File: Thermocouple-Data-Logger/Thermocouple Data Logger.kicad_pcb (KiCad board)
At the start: 4 copper layers, 0 parts

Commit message: Imported all the parts
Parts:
- added C0: 14pF, Capacitors_SMD:C_0402, F.Cu at (201.3, 115.1)
- added C1: 14pF, Capacitors_SMD:C_0402, F.Cu at (205.5, 115.1)
- added C10: 0.01uF, Capacitors_SMD:C_0402, F.Cu at (252.1, 46.7)
- added C11: 0.01uF, Capacitors_SMD:C_0402, F.Cu at (223.6, 72.4)
- added C12: 0.01uF, Capacitors_SMD:C_0402, F.Cu at (220.0, 103.8)
- added C13: 0.1uF, Capacitors_SMD:C_0603, F.Cu at (182.8, 100.7)
- added C14: 0.1uF, Capacitors_SMD:C_0603, F.Cu at (139.4, 124.8)
- added C15: 0.1uF, Capacitors_SMD:C_0603, F.Cu at (257.3, 56.1)
- added C16: 0.1uF, Capacitors_SMD:C_0603, F.Cu at (262.9, 52.0)
- added C17: 0.1uF, Capacitors_SMD:C_0603, F.Cu at (250.8, 61.6)
- added C18: 0.1uF, Capacitors_SMD:C_0603, F.Cu at (240.0, 72.6)
- added C19: 0.1uF, Capacitors_SMD:C_0603, F.Cu at (160.7, 86.8)
- added C2: 18pF, Capacitors_SMD:C_0402, F.Cu at (169.1, 116.4)
- added C20: 0.1uF, Capacitors_SMD:C_0603, F.Cu at (173.5, 86.7)
- added C21: 0.33uF, Capacitors_SMD:C_0603, F.Cu at (169.0, 106.5)
- added C22: 0.33uF, Capacitors_SMD:C_0603, F.Cu at (174.7, 106.5)
- added C23: 0.33uF, Capacitors_SMD:C_0603, F.Cu at (168.9, 111.6)
- added C24: 0.33uF, Capacitors_SMD:C_0603, F.Cu at (162.8, 114.8)
- added C25: 0.33uF, Capacitors_SMD:C_0603, F.Cu at (246.5, 47.0)
- added C26: 0.33uF, Capacitors_SMD:C_0603, F.Cu at (245.7, 63.5)
- added C27: 0.33uF, Capacitors_SMD:C_0603, F.Cu at (252.1, 56.6)
- added C28: 0.33uF, Capacitors_SMD:C_0603, F.Cu at (212.3, 72.6)
- added C29: 0.33uF, Capacitors_SMD:C_0603, F.Cu at (263.4, 47.0)
- added C3: 18pF, Capacitors_SMD:C_0402, F.Cu at (179.6, 110.4)
- added C30: 0.33uF, Capacitors_SMD:C_0603, F.Cu at (252.1, 51.5)
- added C31: 0.33uF, Capacitors_SMD:C_0603, F.Cu at (245.7, 68.5)
- added C32: 0.33uF, Capacitors_SMD:C_0603, F.Cu at (217.9, 72.6)
- added C33: 0.33uF, Capacitors_SMD:C_0603, F.Cu at (177.7, 100.7)
- added C34: 0.33uF, Capacitors_SMD:C_0603, F.Cu at (155.9, 123.3)
- added C35: 0.33uF, Capacitors_SMD:C_0603, F.Cu at (172.7, 70.1)
- added C36: 0.33uF, Capacitors_SMD:C_0603, F.Cu at (181.1, 65.3)
- added C37: 0.33uF, Capacitors_SMD:C_0603, F.Cu at (172.7, 75.1)
- added C38: 0.33uF, Capacitors_SMD:C_0603, F.Cu at (161.2, 81.7)
- added C39: 0.33uF, Capacitors_SMD:C_0603, F.Cu at (199.4, 47.0)
- added C4: 0.01uF, Capacitors_SMD:C_0402, F.Cu at (257.8, 51.3)
- added C40: 10uF, Capacitors_SMD:C_1210, F.Cu at (204.2, 105.9)
- added C41: 22uf, Capacitors_SMD:C_1206, F.Cu at (214.7, 104.2)
- added C5: 0.01uF, Capacitors_SMD:C_0402, F.Cu at (234.8, 72.4)
- added C6: 0.01uF, Capacitors_SMD:C_0402, F.Cu at (257.8, 46.7)
- added C7: 0.01uF, Capacitors_SMD:C_0402, F.Cu at (246.5, 56.4)
- added C8: 0.01uF, Capacitors_SMD:C_0402, F.Cu at (229.2, 72.4)
- added C9: 0.01uF, Capacitors_SMD:C_0402, F.Cu at (246.5, 51.8)
- added D0: LED Power, LEDs:LED_0603, F.Cu at (161.8, 109.9)
- added D1: LED Debug, LEDs:LED_0603, F.Cu at (161.9, 105.2)
- added D10: D_Schottky, Diodes_SMD:D_SOD-323, F.Cu at (179.1, 95.3)
- added D11: D_Schottky, Diodes_SMD:D_SOD-323, F.Cu at (170.4, 101.1)
- added D2: LED Probe 1, LEDs:LED_0603, F.Cu at (174.9, 46.7)
- added D3: LED Probe 2, LEDs:LED_0603, F.Cu at (174.9, 51.4)
- added D4: LED Probe 3, LEDs:LED_0603, F.Cu at (174.9, 56.0)
- added D5: LED Probe 4, LEDs:LED_0603, F.Cu at (155.0, 76.8)
- added D6: LED °C, LEDs:LED_0603, F.Cu at (162.9, 76.8)
- added D7: LED °F, LEDs:LED_0603, F.Cu at (191.1, 55.9)
- added D8: LED K, LEDs:LED_0603, F.Cu at (199.3, 79.4)
- added D9: D_Schottky, Diodes_SMD:D_SOD-323, F.Cu at (170.4, 95.3)
- added J0: Power, Connectors_JST:JST_PH_S2B-PH-SM4-TB_02x2.00mm_Angled, F.Cu at (196.9, 99.1)
- added J1: Micro_SD_Card_Det, Connectors_Card:Hirose_DM3BT-DSF-PEJS, F.Cu at (87.0, 84.0)
- added J2: Probe 1, TerminalBlock-PTSA:TeaminalBlock_Phonix_PTSA-3.5mm_2pol, F.Cu at (85.0, 30.0)
- added J3: Probe 2, TerminalBlock-PTSA:TeaminalBlock_Phonix_PTSA-3.5mm_2pol, F.Cu at (105.0, 30.0)
- added J4: Probe 3, TerminalBlock-PTSA:TeaminalBlock_Phonix_PTSA-3.5mm_2pol, F.Cu at (125.0, 30.0)
- added J5: Probe 4, TerminalBlock-PTSA:TeaminalBlock_Phonix_PTSA-3.5mm_2pol, F.Cu at (145.0, 30.0)
- added J6: ISP, Pin_Headers:Pin_Header_Straight_2x03_Pitch2.54mm, F.Cu at (85.0, 107.3)
- added R0: 100, Resistors_SMD:R_0603, F.Cu at (254.9, 61.6)
- added R1: 100, Resistors_SMD:R_0603, F.Cu at (244.1, 73.5)
- added R10: 200, Resistors_SMD:R_0805, F.Cu at (161.7, 120.0)
- added R11: 200, Resistors_SMD:R_0805, F.Cu at (192.7, 66.4)
- added R12: 200, Resistors_SMD:R_0805, F.Cu at (187.9, 71.8)
- added R13: 200, Resistors_SMD:R_0805, F.Cu at (202.8, 58.0)
- added R14: 200, Resistors_SMD:R_0805, F.Cu at (177.3, 70.5)
- added R15: 200, Resistors_SMD:R_0805, F.Cu at (181.8, 81.8)
- added R16: 200, Resistors_SMD:R_0805, F.Cu at (196.3, 68.5)
- added R17: 200, Resistors_SMD:R_0805, F.Cu at (191.5, 71.8)
- added R18: 200, Resistors_SMD:R_0805, F.Cu at (187.9, 77.3)
- added R19: 200, Resistors_SMD:R_0805, F.Cu at (199.8, 63.5)
- added R2: 100, Resistors_SMD:R_0603, F.Cu at (250.2, 71.6)
- added R20: 200, Resistors_SMD:R_0805, F.Cu at (203.4, 63.5)
- added R21: 200, Resistors_SMD:R_0805, F.Cu at (199.8, 68.9)
- added R22: 200, Resistors_SMD:R_0805, F.Cu at (191.5, 77.3)
- added R23: 200, Resistors_SMD:R_0805, F.Cu at (195.0, 74.0)
- added R24: 200, Resistors_SMD:R_0805, F.Cu at (185.3, 82.7)
- added R25: 200, Resistors_SMD:R_0805, F.Cu at (203.4, 68.9)
- added R26: 200, Resistors_SMD:R_0805, F.Cu at (188.9, 82.7)
- added R27: 200, Resistors_SMD:R_0805, F.Cu at (198.6, 74.4)
- added R28: 200, Resistors_SMD:R_0805, F.Cu at (195.0, 79.4)
- added R29: 200, Resistors_SMD:R_0805, F.Cu at (202.1, 74.4)
- added R3: 100, Resistors_SMD:R_0603, F.Cu at (250.2, 66.6)
- added R30: 200, Resistors_SMD:R_0805, F.Cu at (169.3, 85.8)
- added R31: 200, Resistors_SMD:R_0805, F.Cu at (204.0, 47.1)
- added R32: 200, Resistors_SMD:R_0805, F.Cu at (198.4, 52.2)
- added R33: 200, Resistors_SMD:R_0805, F.Cu at (190.0, 60.9)
- added R34: 200, Resistors_SMD:R_0805, F.Cu at (185.6, 65.4)
- added R35: 200, Resistors_SMD:R_0805, F.Cu at (165.8, 82.7)
- added R36: 200, Resistors_SMD:R_0805, F.Cu at (196.3, 63.1)
- added R37: 200, Resistors_SMD:R_0805, F.Cu at (178.2, 81.4)
- added R38: 200, Resistors_SMD:R_0805, F.Cu at (184.4, 76.3)
- added R39: 200, Resistors_SMD:R_0805, F.Cu at (174.7, 81.4)
- added R4: 100, Resistors_SMD:R_0603, F.Cu at (261.3, 57.0)
- added R40: 200, Resistors_SMD:R_0805, F.Cu at (202.8, 52.6)
- added R41: 200, Resistors_SMD:R_0805, F.Cu at (180.8, 75.9)
- added R42: 200, Resistors_SMD:R_0805, F.Cu at (199.2, 57.6)
- added R43: 200, Resistors_SMD:R_0805, F.Cu at (167.6, 77.2)
- added R44: 200, Resistors_SMD:R_0805, F.Cu at (189.2, 66.4)
- added R45: 200, Resistors_SMD:R_0805, F.Cu at (195.7, 57.6)
- added R46: 200, Resistors_SMD:R_0805, F.Cu at (184.4, 70.9)
- added R47: 200, Resistors_SMD:R_0805, F.Cu at (177.3, 75.9)
- added R48: 200, Resistors_SMD:R_0805, F.Cu at (180.8, 70.5)
- added R49: 200, Resistors_SMD:R_0805, F.Cu at (171.1, 80.3)
- added R5: 100, Resistors_SMD:R_0603, F.Cu at (264.7, 57.0)
- added R50: 1k, Resistors_SMD:R_0402, F.Cu at (177.5, 86.5)
- added R51: 1k, Resistors_SMD:R_0402, F.Cu at (181.0, 86.9)
- added R52: 10k, Resistors_SMD:R_0402, F.Cu at (173.4, 111.4)
- added R53: 10k, Resistors_SMD:R_0402, F.Cu at (165.2, 119.7)
- added R54: 10k, Resistors_SMD:R_0402, F.Cu at (179.2, 105.6)
- added R55: 10k, Resistors_SMD:R_0402, F.Cu at (192.4, 84.6)
- added R56: 10k, Resistors_SMD:R_0402, F.Cu at (195.8, 84.6)
- added R57: 470k, Resistors_SMD:R_0402, F.Cu at (160.8, 125.1)
- added R58: 470k, Resistors_SMD:R_0402, F.Cu at (173.8, 116.3)
- added R59: 470k, Resistors_SMD:R_0402, F.Cu at (183.0, 105.6)
- added R6: 100, Resistors_SMD:R_0603, F.Cu at (253.6, 66.6)
- added R7: 100, Resistors_SMD:R_0603, F.Cu at (258.3, 62.0)
- added R8: 200, Resistors_SMD:R_0805, F.Cu at (185.3, 95.1)
- added R9: 200, Resistors_SMD:R_0805, F.Cu at (138.8, 119.5)
- added SW0: Power, Buttons_Switches_SMD:SW_SPDT_CK-JS102011SAQN, F.Cu at (207.0, 98.2)
- added SW1: Display, Buttons_Switches_SMD:SW_SPDT_CK-JS102011SAQN, F.Cu at (147.9, 121.6)
- added SW2: Reset, Buttons_Switches_SMD:SW_SPST_PTS645, F.Cu at (131.8, 121.9)
- added SW3: Select/Calibrate, Buttons_Switches_SMD:SW_SPST_PTS645, F.Cu at (133.0, 79.6)
- added SW4: Cycle/Menu, Buttons_Switches_SMD:SW_SPST_PTS645, F.Cu at (144.7, 79.6)
- added SW5: SW_DIP_x04, Buttons_Switches_SMD:SW_DIP_x4_W5.08mm_Slide_Copal_CHS-A, F.Cu at (161.5, 97.7)
- added U0: ATMEGA324PA-MU, Housings_DFN_QFN:QFN-44-1EP_7x7mm_Pitch0.5mm, F.Cu at (104.4, 83.1)
- added U1: LT1763-3.3, Housings_SOIC:SOIC-8_3.9x4.9mm_Pitch1.27mm, F.Cu at (217.0, 96.9)
- added U10: 74HC595, Housings_SSOP:TSSOP-16_4.4x5mm_Pitch0.65mm, F.Cu at (184.1, 49.0)
- added U11: HDSP-521E-Display, Display:HDSP-521E, F.Cu at (74.0, 62.5)
- added U12: HDSP-521E-Display, Display:HDSP-521E, F.Cu at (99.5, 62.5)
- added U13: 4050, Housings_SSOP:TSSOP-16_4.4x5mm_Pitch0.65mm, F.Cu at (153.4, 108.5)
- added U2: MAX31856, Housings_SSOP:TSSOP-14_4.4x5mm_Pitch0.65mm, F.Cu at (85.0, 40.0)
- added U3: MAX31856, Housings_SSOP:TSSOP-14_4.4x5mm_Pitch0.65mm, F.Cu at (105.0, 40.0)
- added U4: MAX31856, Housings_SSOP:TSSOP-14_4.4x5mm_Pitch0.65mm, F.Cu at (125.0, 40.0)
- added U5: MAX31856, Housings_SSOP:TSSOP-14_4.4x5mm_Pitch0.65mm, F.Cu at (145.0, 40.0)
- added U6: 74HC595, Housings_SSOP:TSSOP-16_4.4x5mm_Pitch0.65mm, F.Cu at (154.2, 83.8)
- added U7: 74HC595, Housings_SSOP:TSSOP-16_4.4x5mm_Pitch0.65mm, F.Cu at (192.4, 49.0)
- added U8: 74HC595, Housings_SSOP:TSSOP-16_4.4x5mm_Pitch0.65mm, F.Cu at (184.1, 58.2)
- added U9: 74HC595, Housings_SSOP:TSSOP-16_4.4x5mm_Pitch0.65mm, F.Cu at (174.1, 63.0)
- added Y0: 10MHz, Crystals:Crystal_SMD_Abracon_ABM3B-4pin_5.0x3.2mm, F.Cu at (156.5, 116.9)
- added Y1: 32.768KHz, Crystals:Crystal_DS26_d2.0mm_l6.0mm_Horizontal, F.Cu at (194.6, 115.6)
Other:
- rule pad_to_mask_clearance: 0.2 -> 0

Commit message: Started laying out components
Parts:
- moved C4 174.3 mm to (84.3, 34.5)
- moved R0 173.6 mm to (83.8, 31.9), turned to 180 degrees
- moved C15 173.5 mm to (85.3, 33.3)
- moved C26 164.8 mm to (82.0, 44.3), turned to 180 degrees
- moved C25 163.5 mm to (83.3, 35.7), turned to 180 degrees
- moved R1 162.6 mm to (86.8, 31.9)
- moved C5 153.3 mm to (86.3, 34.5)
- moved C27 150.2 mm to (103.3, 35.6), turned to 180 degrees
- moved R2 146.9 mm to (108.7, 32.3)
- moved C29 140.5 mm to (123.3, 35.7), turned to 180 degrees
- moved R4 134.1 mm to (129.5, 32.5), turned to 90 degrees
- moved C30 130.3 mm to (122.0, 44.3), turned to 180 degrees
- moved C17 128.0 mm to (126.4, 31.8)
- moved C28 113.8 mm to (102.0, 44.3), turned to 180 degrees
- moved R7 111.2 mm to (151.2, 31.7)
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
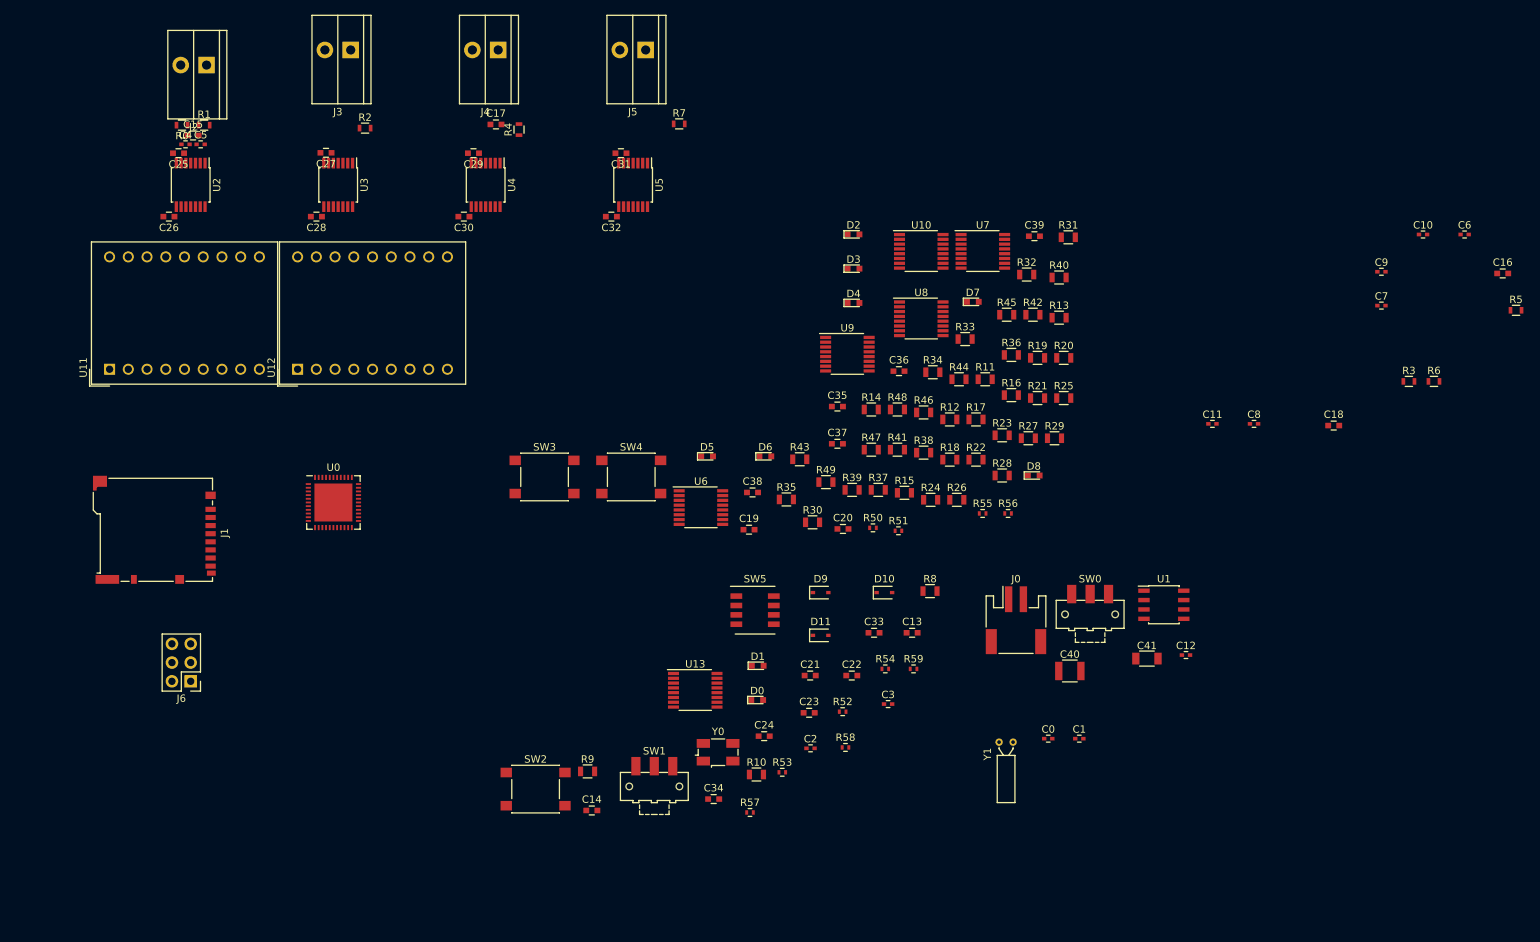
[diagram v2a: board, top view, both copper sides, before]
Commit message: Made thermocouple input layout
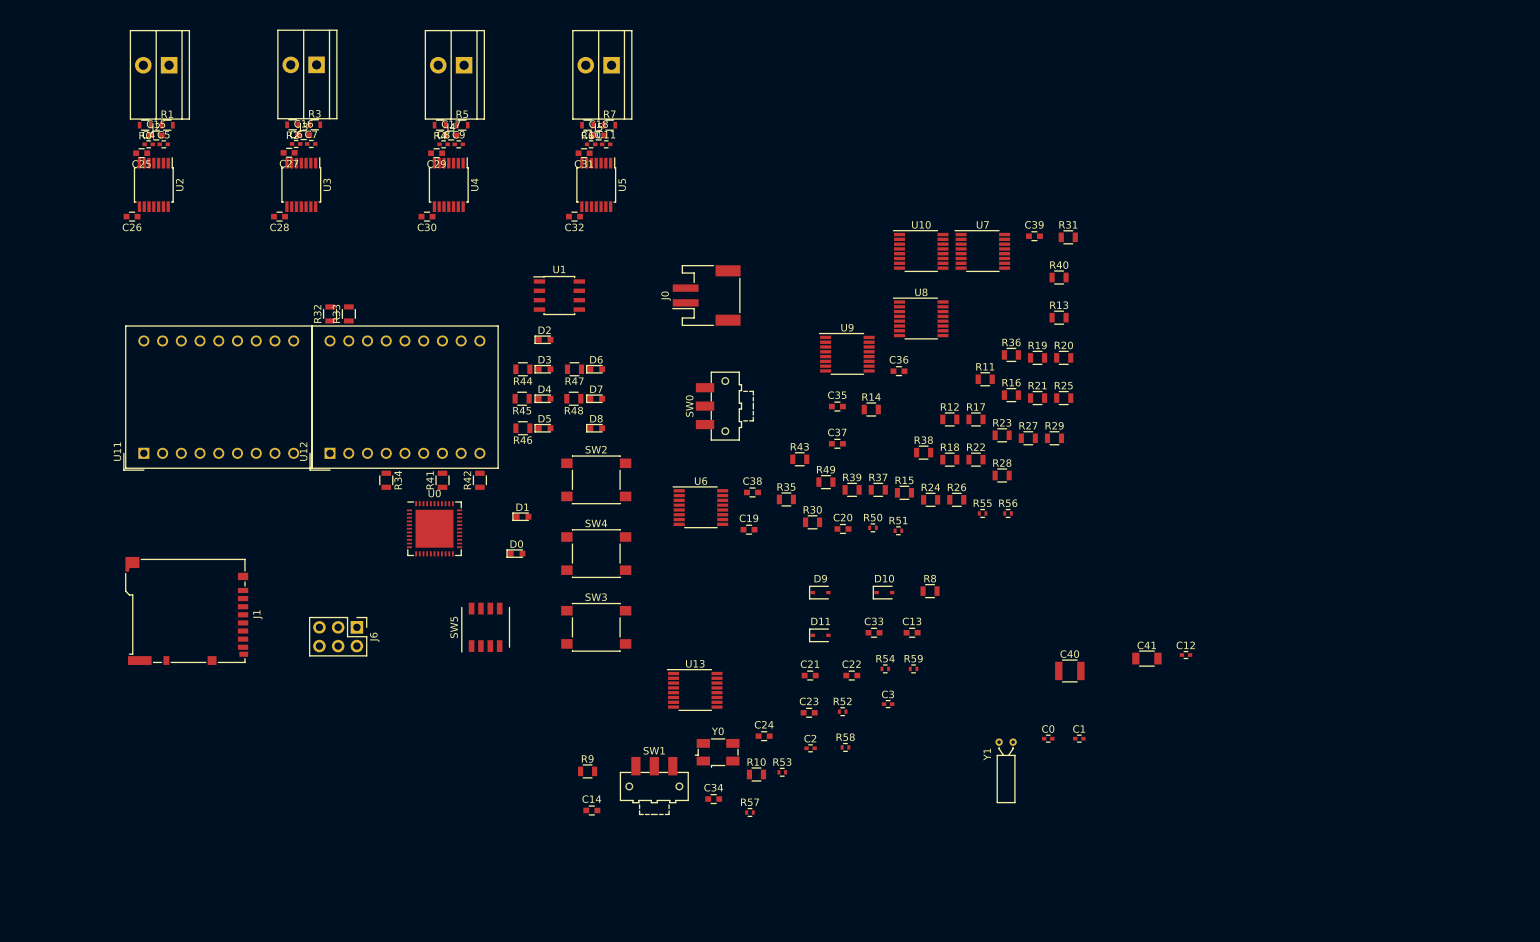
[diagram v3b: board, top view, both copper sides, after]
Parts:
- moved C16 163.7 mm to (100.3, 33.2)
- moved C6 158.9 mm to (99.3, 34.5)
- moved R3 152.4 mm to (101.8, 31.9)
- moved C7 146.8 mm to (101.3, 34.5)
- moved R5 145.1 mm to (121.8, 31.9)
- moved C9 126.3 mm to (121.3, 34.5)
- moved R6 119.9 mm to (138.8, 31.9), turned to 180 degrees
- moved C8 116.3 mm to (119.3, 34.5)
- moved C10 113.5 mm to (139.3, 34.5)
- moved C18 107.2 mm to (140.3, 33.3)
- moved R32 94.6 mm to (103.9, 57.5), turned to 90 degrees
- moved U1 92.1 mm to (135.0, 55.0)
- moved C11 90.5 mm to (141.3, 34.5)
- moved R33 83.6 mm to (106.5, 57.5), turned to 90 degrees
- moved R42 78.3 mm to (124.2, 80.1), turned to 90 degrees
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
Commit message: Added mounting holes, grounding holes and fiducials
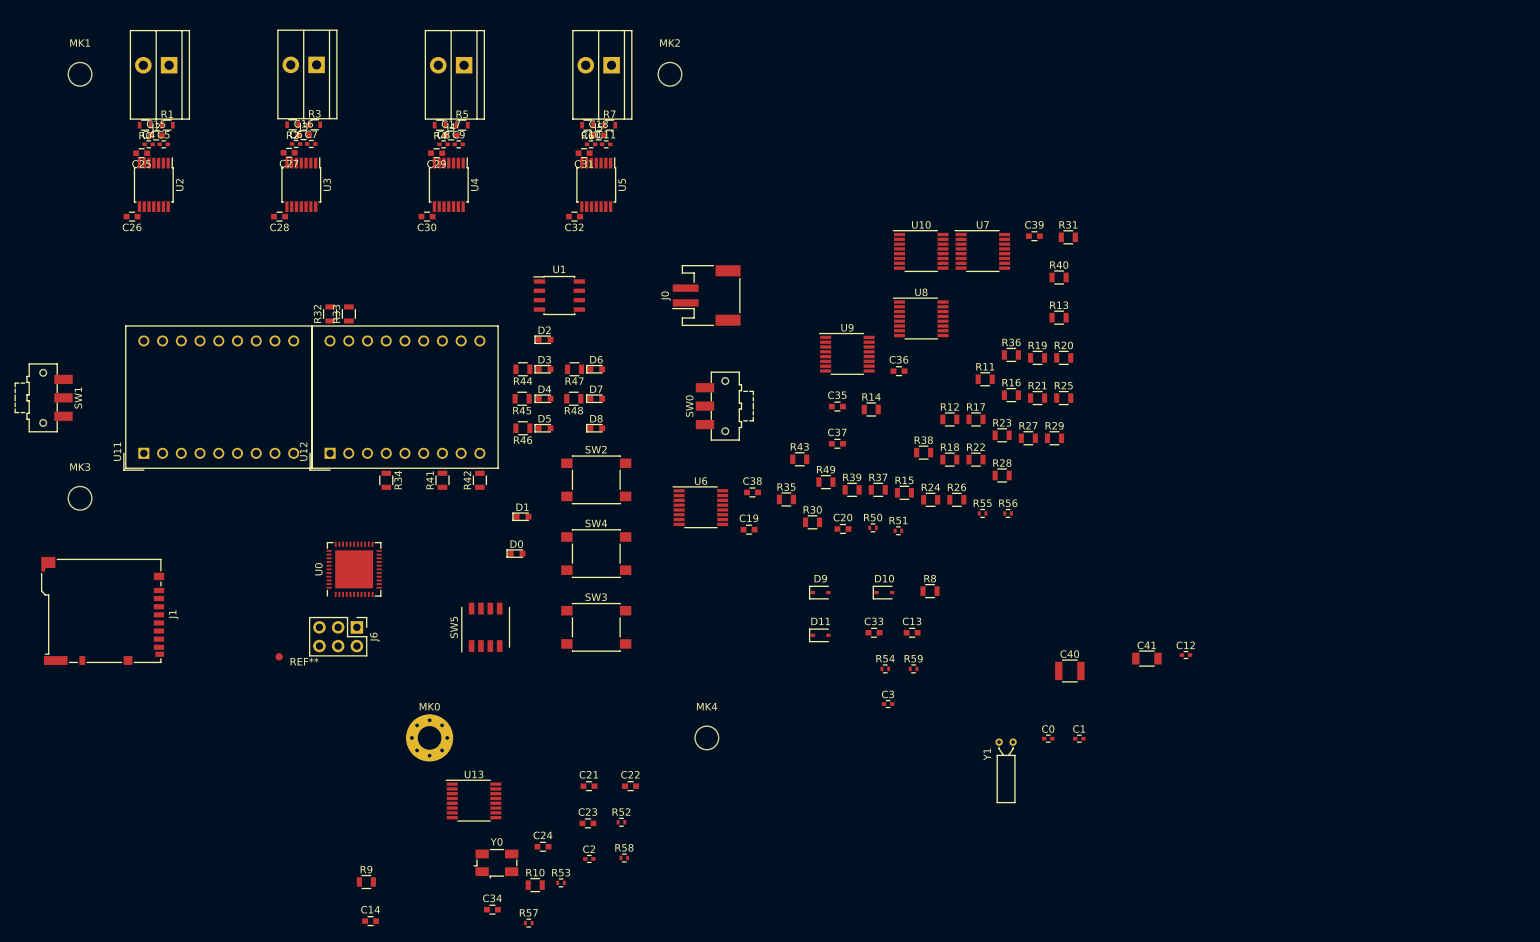
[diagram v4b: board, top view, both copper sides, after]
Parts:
- added MK0: Mounting_Hole_PAD, Mounting_Holes:MountingHole_3.2mm_M3_Pad_Via, F.Cu at (117.4, 115.0)
- added MK1: Mounting_Hole, Mounting_Holes:MountingHole_3.2mm_M3, F.Cu at (70.0, 25.0)
- added MK2: Mounting_Hole, Mounting_Holes:MountingHole_3.2mm_M3, F.Cu at (150.0, 25.0)
- added MK3: Mounting_Hole, Mounting_Holes:MountingHole_3.2mm_M3, F.Cu at (70.0, 82.5)
- added MK4: Mounting_Hole, Mounting_Holes:MountingHole_3.2mm_M3, F.Cu at (155.0, 115.0)
- added REF**: Fiducial_1mm_Dia_2.54mm_Outer_CopperTop, Fiducials:Fiducial_1mm_Dia_2.54mm_Outer_CopperTop, F.Cu at (97.0, 104.0)
- moved SW1 98.2 mm to (65.0, 68.9), turned to 270 degrees
- moved U13 33.5 mm to (123.4, 123.5)
- moved C2 33.5 mm to (139.1, 131.4)
- moved C21 33.5 mm to (139.0, 121.5)
- moved C22 33.5 mm to (144.7, 121.5)
- moved C23 33.5 mm to (138.9, 126.6)
- moved C24 33.5 mm to (132.8, 129.8)
- moved C34 33.5 mm to (125.9, 138.3)
- moved R10 33.5 mm to (131.7, 135.0)
- moved R52 33.5 mm to (143.4, 126.4)
- moved R53 33.5 mm to (135.2, 134.7)
- moved R58 33.5 mm to (143.8, 131.3)
- moved Y0 33.5 mm to (126.5, 131.9)
- moved R57 33.5 mm to (130.8, 140.1)
- moved C14 33.5 mm to (109.4, 139.8)
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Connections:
- U0 pad 45: GND -> (no net)

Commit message: Finished general layout of large components
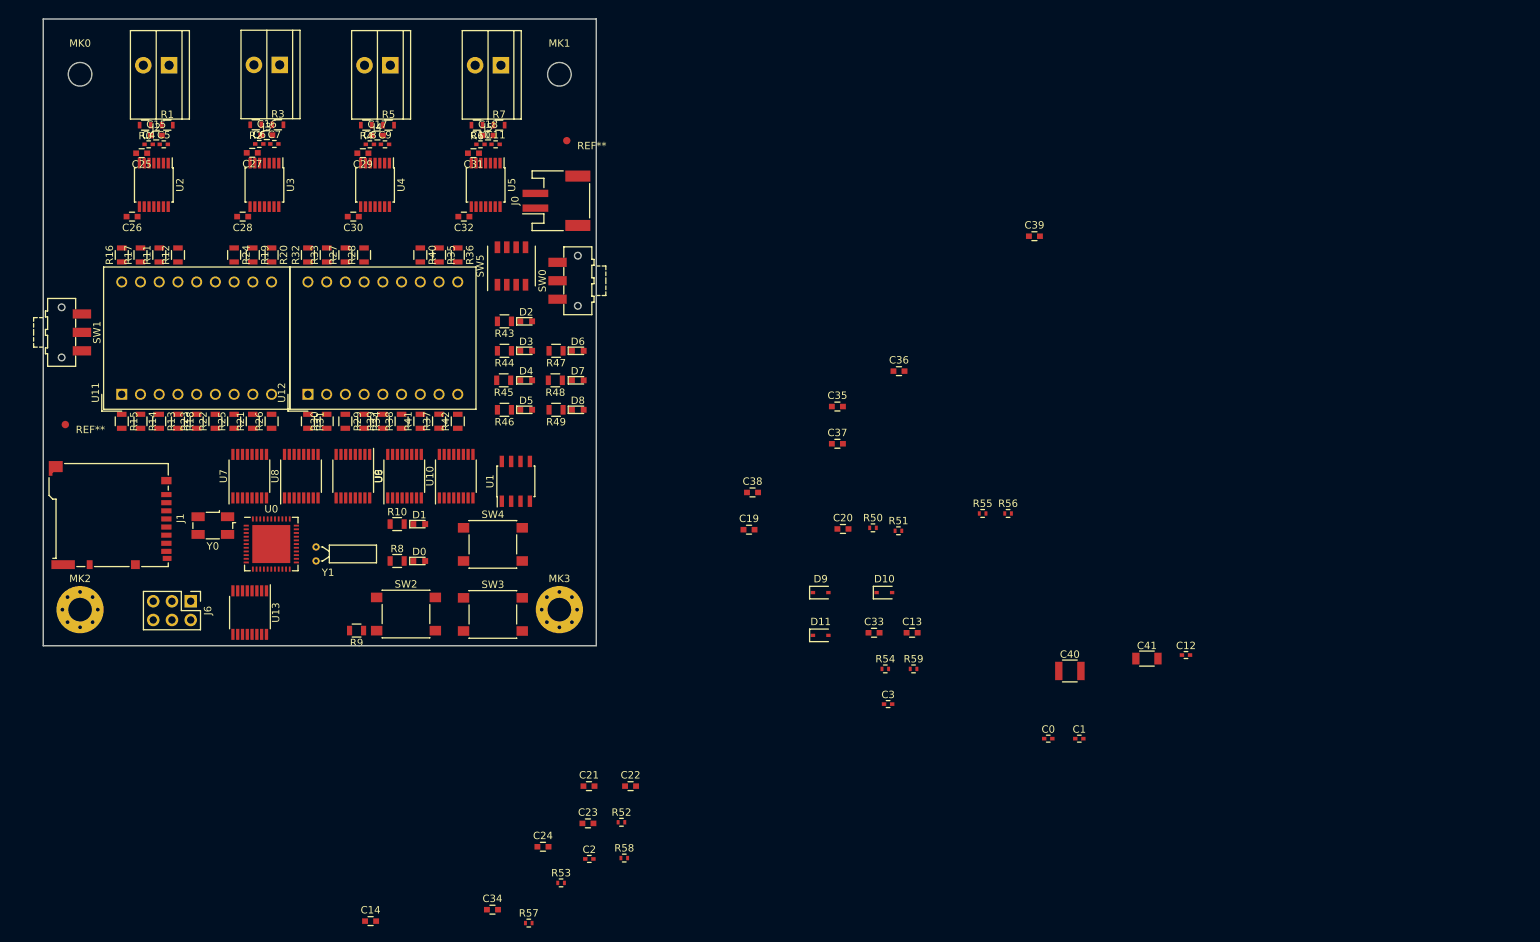
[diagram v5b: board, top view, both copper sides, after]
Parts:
- removed MK4: Mounting_Hole, Mounting_Holes:MountingHole_3.2mm_M3
- removed the REF** at (97.0, 104.0)
- added REF**: Fiducial_1mm_Dia_2.54mm_Outer_CopperTop, Fiducials:Fiducial_1mm_Dia_2.54mm_Outer_CopperTop, F.Cu at (136.0, 34.0)
- added REF**: Fiducial_1mm_Dia_2.54mm_Outer_CopperTop, Fiducials:Fiducial_1mm_Dia_2.54mm_Outer_CopperTop, F.Cu at (68.0, 72.5)
- MK0: value Mounting_Hole_PAD -> Mounting_Hole; footprint Mounting_Holes:MountingHole_3.2mm_M3_Pad_Via -> Mounting_Holes:MountingHole_3.2mm_M3
- MK2, MK3: value Mounting_Hole -> Mounting_Hole_PAD; footprint Mounting_Holes:MountingHole_3.2mm_M3 -> Mounting_Holes:MountingHole_3.2mm_M3_Pad_Via
- moved R13 122.8 mm to (80.7, 72.1), turned to 270 degrees
- moved R16 122.1 mm to (75.7, 49.5), turned to 90 degrees
- moved R17 115.5 mm to (78.2, 49.5), turned to 90 degrees
- moved R11 113.3 mm to (80.7, 49.5), turned to 90 degrees
- moved R25 112.5 mm to (90.9, 72.1), turned to 90 degrees
- moved R23 109.3 mm to (85.8, 72.1), turned to 90 degrees
- moved R20 108.3 mm to (96.0, 49.5), turned to 270 degrees
- moved MK2 108.0 mm to (70.0, 97.6)
- moved R19 107.3 mm to (93.4, 49.5), turned to 270 degrees
- moved R12 107.0 mm to (83.3, 49.5), turned to 90 degrees
- moved R15 106.6 mm to (75.7, 72.1), turned to 270 degrees
- moved R21 106.5 mm to (93.4, 72.1), turned to 90 degrees
- moved R31 106.1 mm to (100.9, 72.1), turned to 270 degrees
- moved R18 104.8 mm to (83.3, 72.1), turned to 270 degrees
- moved U7 104.0 mm to (93.0, 79.5), turned to 90 degrees
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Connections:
- MK2 pad 1: (no net) -> GND
- MK3 pad 1: (no net) -> GND
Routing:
- added copper zone on In2.Cu, net +3V3
- added copper zone on In2.Cu, net /Thermocouple/VCC3
- added copper zone on In2.Cu, net /Thermocouple/VCC4
- added copper zone on In2.Cu, net DD
- added copper zone on In1.Cu, net GND
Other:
- board outline added: 75 x 85 mm
